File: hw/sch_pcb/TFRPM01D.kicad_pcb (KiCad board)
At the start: 2 copper layers, 37.5 x 19 mm, 28 parts, among them J1 HEADER_1x03, J2 SM04B-GHS-TB, J3 SM04B-GHS-TB, M2 M3, U1 PCF8583, U2 SN74LVC1G14-Q1, U3 MIC5504-3.3YM5

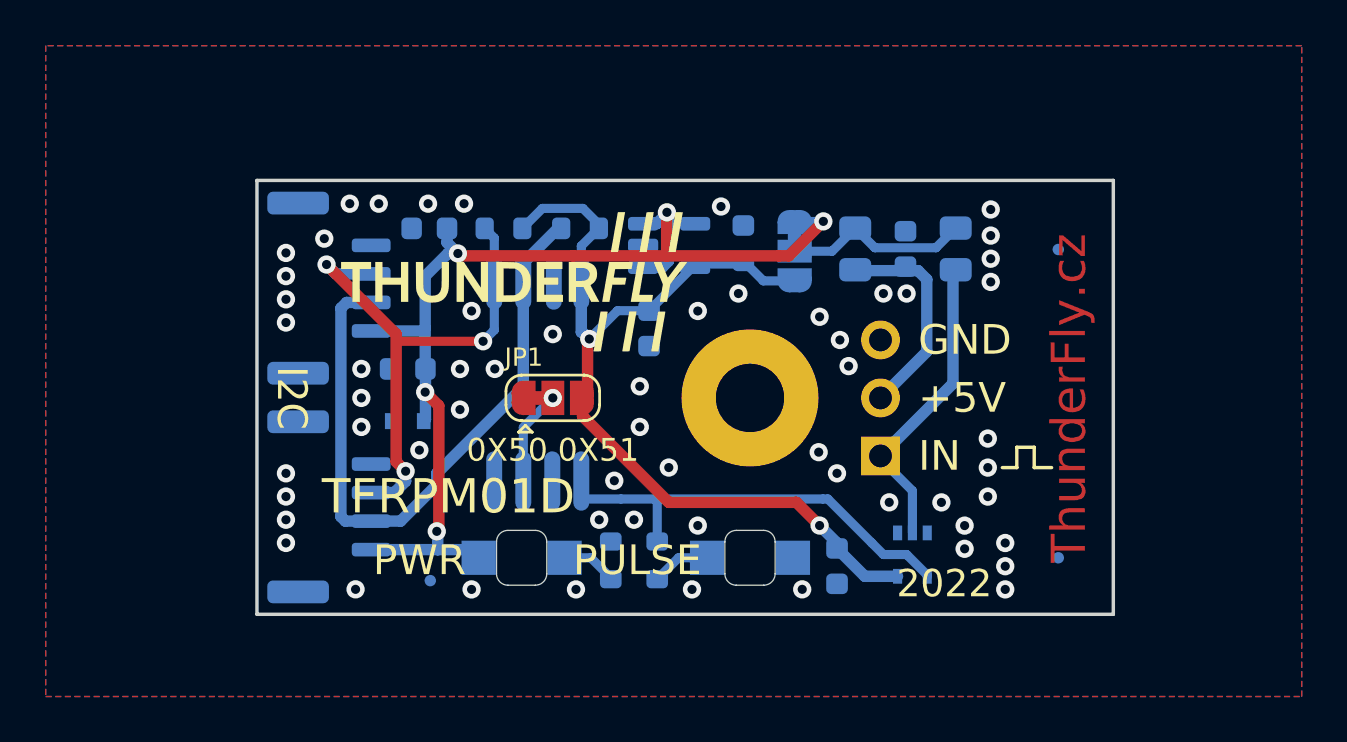
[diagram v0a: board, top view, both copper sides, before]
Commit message: Graphics and layout improvements. Net classes for default and power set.
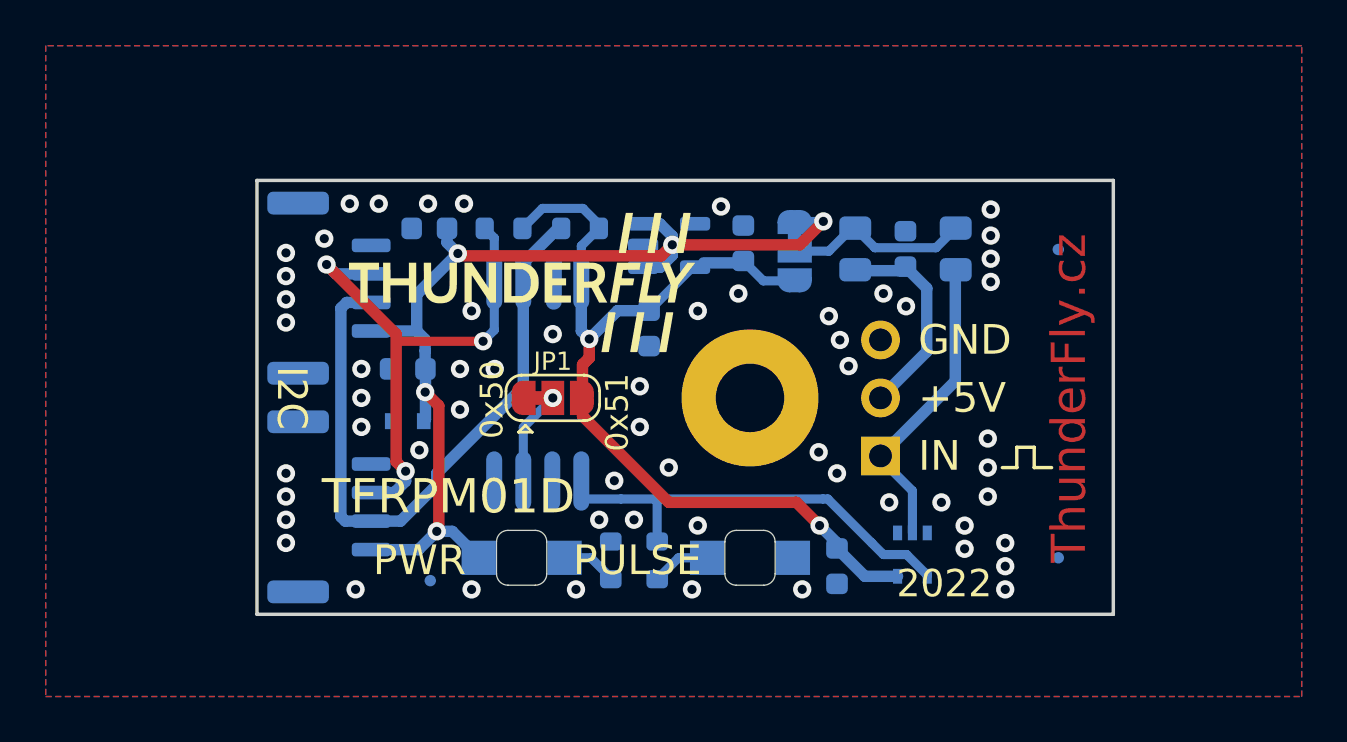
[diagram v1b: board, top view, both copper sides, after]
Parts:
- moved G1 0.35 mm to (122.5, 127.3)
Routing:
- net +5V: track 49.5 -> 46.2 mm
- net +3V3: track 39.6 -> 41.0 mm
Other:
- board text added: "0x50"
- board text added: "0x51"
- board text removed: "0X50 0X51"

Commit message: Repair #30
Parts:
- moved C2 0.27 mm to (139.2, 126.0)
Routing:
- net +5V: track 46.2 -> 43.7 mm
- net /SCL: track 29.7 -> 31.7 mm
- net +3V3: track 41.0 -> 40.4 mm
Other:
- board text added: "0x50 0x51"
- board text removed: "0x50"
- board text removed: "0x51"

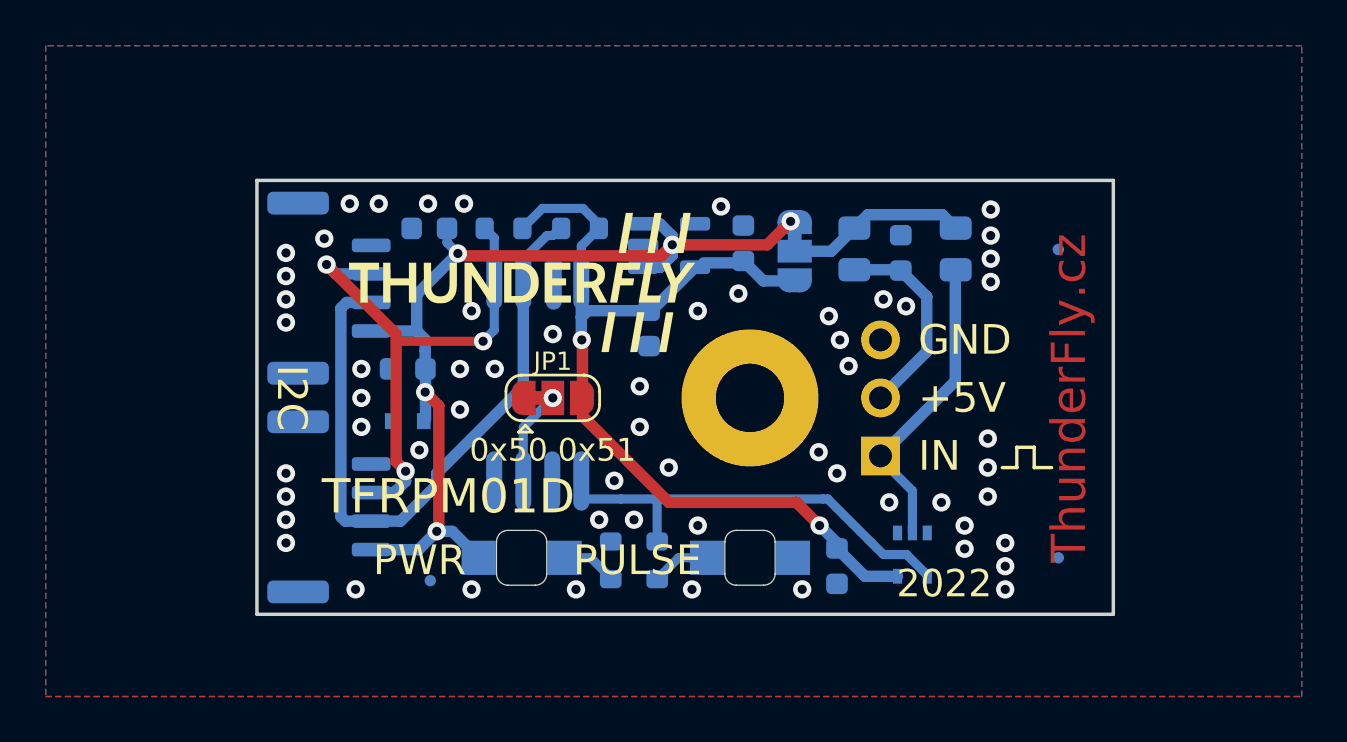
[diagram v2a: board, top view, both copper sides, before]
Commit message: Silkscreen modification
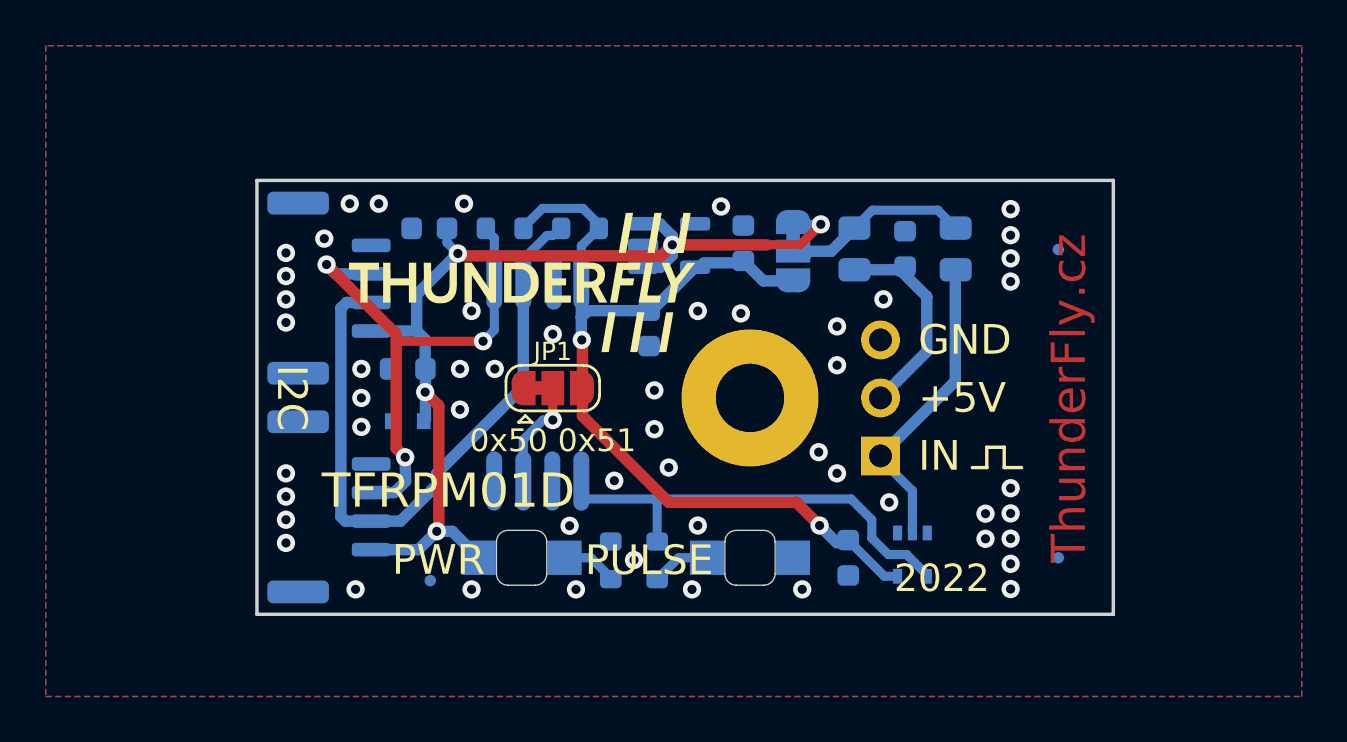
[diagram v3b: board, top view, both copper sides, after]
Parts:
- moved C6 0.61 mm to (136.9, 139.3)
- moved JP1 0.43 mm to (124.0, 131.9)
- moved C2 0.26 mm to (139.4, 125.8)
- moved JP2 0.07 mm to (134.5, 125.9)
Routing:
- net /SCL: track 31.7 -> 27.4 mm
- net +5V: track 43.7 -> 44.8 mm
- net +3V3: track 40.4 -> 39.4 mm
- net Net-(JP1-Pad2): track 4.17 -> 4.86 mm
- net GND: vias 58 -> 52

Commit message: Improve silkscreen.
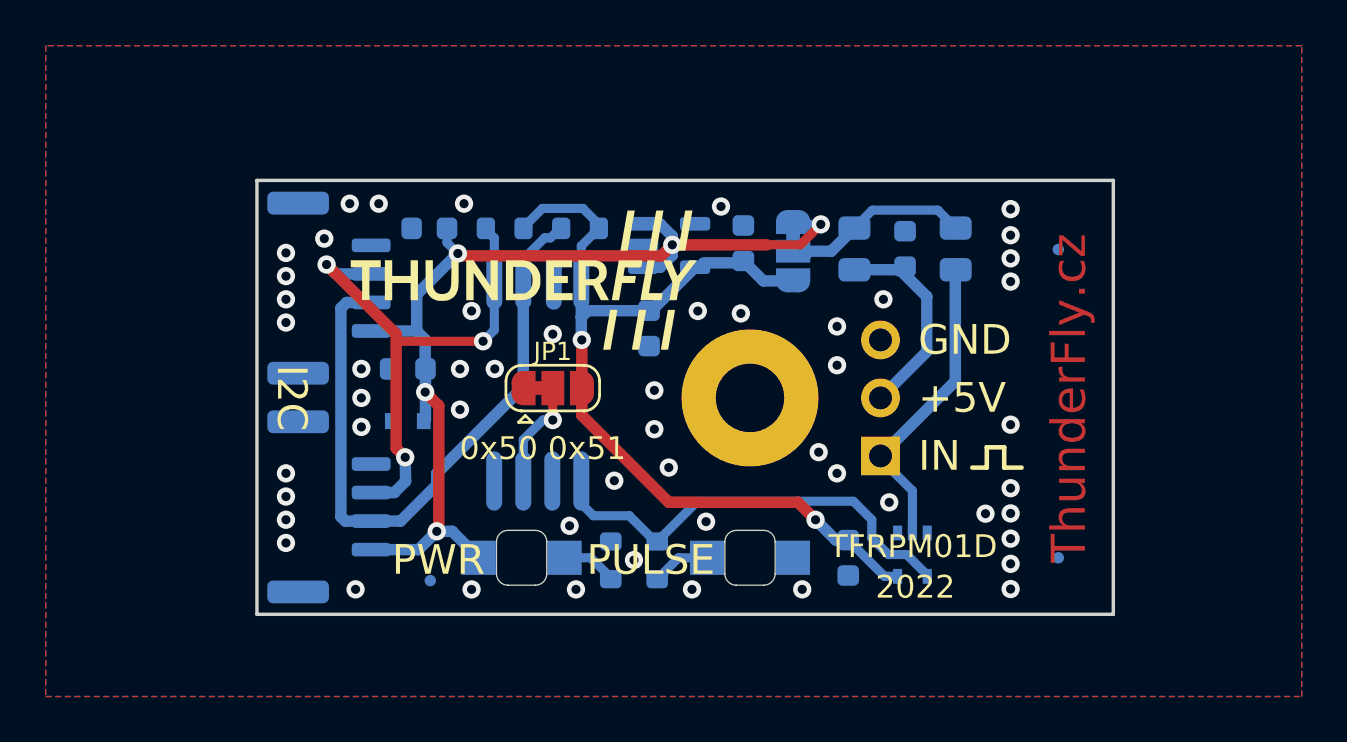
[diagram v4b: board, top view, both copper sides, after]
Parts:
- moved G1 0.13 mm to (122.6, 127.2)
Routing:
- net Net-(R4-Pad1): track 18.9 -> 19.6 mm

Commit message: Improve layout uniform track widts. Resolve DRC and ERC issues.
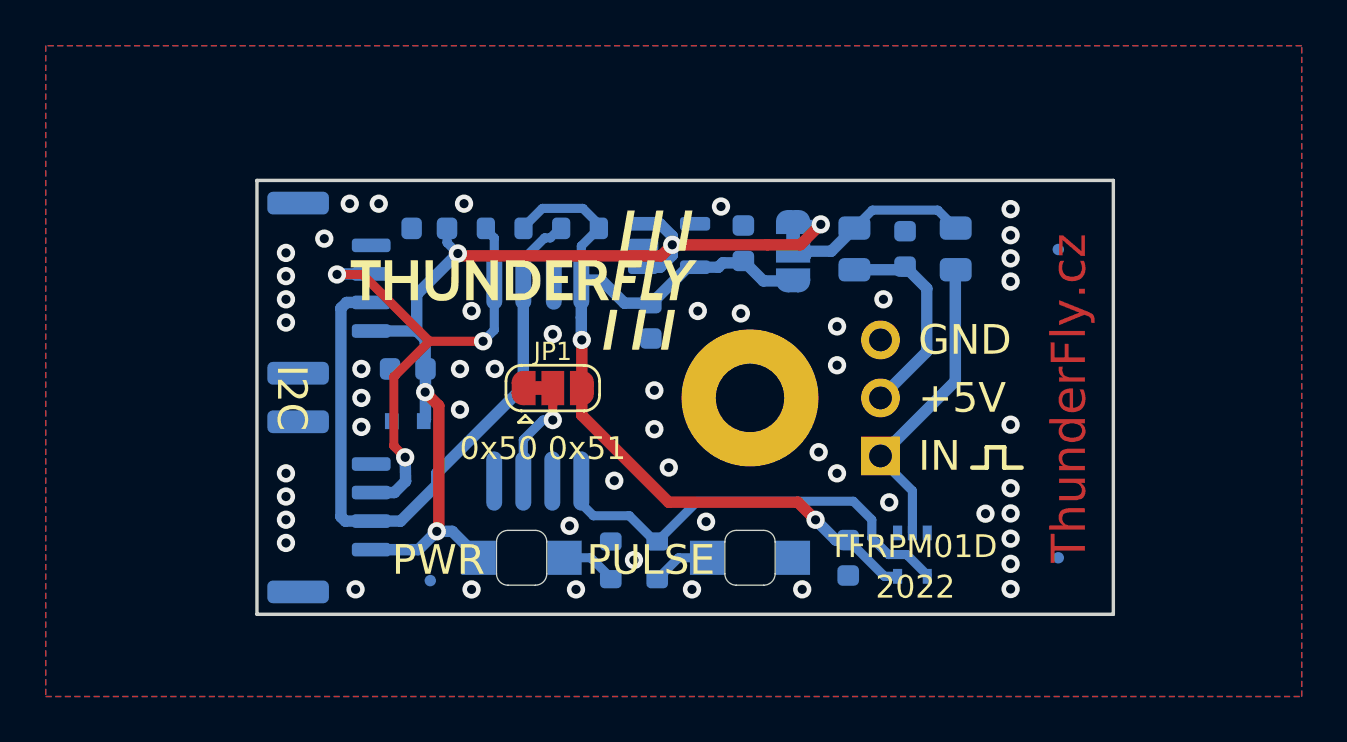
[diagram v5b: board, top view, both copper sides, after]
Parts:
- moved C5 0.34 mm to (128.2, 129.0)
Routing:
- net +3V3: track 39.9 -> 40.6 mm
- net /SDA: track 23.7 -> 23.1 mm
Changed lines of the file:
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@@
   )
   (footprint "Capacitor_SMD:C_0603_1608Metric" (layer "B.Cu")
-    (at 128.1685 129.286 -90)
+    (at 128.2446 128.9558 -90)
     (descr "Capacitor SMD 0603 (1608 Metric), square (rectangular) end terminal, IPC_7351 nominal, (Body size source: IPC-SM-782 page 76, https://www.pcb-3d.com/wordpress/wp-content/uploads/ipc-sm-782a_amendment_1_and_2.pdf), generated with kicad-footprint-generator")
     (tags "capacitor")
@@
   (via (at 125.222 129.791096) (size 0.8) (drill 0.4) (layers "F.Cu" "B.Cu") (net 4))
   (via (at 135.4582 137.668) (size 0.8) (drill 0.4) (layers "F.Cu" "B.Cu") (net 4))
-  (segment (start 125.486096 128.511) (end 125.201 128.796096) (width 0.5) (layer "B.Cu") (net 4))
   (segment (start 125.201 127.956) (end 125.201 125.676) (width 0.4) (layer "B.Cu") (net 4))
+  (segment (start 131.394 126.416) (end 131.999 126.416) (width 0.5) (layer "B.Cu") (net 4))
   (segment (start 125.201 129.770096) (end 125.201 128.796096) (width 0.5) (layer "B.Cu") (net 4))
   (segment (start 125.201 128.796096) (end 125.201 127.169096) (width 0.5) (layer "B.Cu") (net 4))
   (segment (start 139.05 140.142) (end 138.473904 140.142) (width 0.4) (layer "B.Cu") (net 4))
-  (segment (start 130.556 126.416) (end 131.999 126.416) (width 0.5) (layer "B.Cu") (net 4))
+  (segment (start 128.283 128.1808) (end 129.8578 126.606) (width 0.5) (layer "B.Cu") (net 4))
   (segment (start 136.346296 138.556096) (end 135.4582 137.668) (width 0.5) (layer "B.Cu") (net 4))
+  (segment (start 127.0886 128.1808) (end 128.2446 128.1808) (width 0.5) (layer "B.Cu") (net 4))
   (segment (start 125.971 124.731) (end 125.27148 124.03148) (width 0.4) (layer "B.Cu") (net 4))
+  (segment (start 130.1835 126.606) (end 131.204 126.606) (width 0.5) (layer "B.Cu") (net 4))
+  (segment (start 129.8578 126.606) (end 130.1835 126.606) (width 0.5) (layer "B.Cu") (net 4))
   (segment (start 134.546 127.206) (end 133.171 127.206) (width 0.5) (layer "B.Cu") (net 4))
   (segment (start 125.27148 124.03148) (end 123.49552 124.03148) (width 0.4) (layer "B.Cu") (net 4))
+  (segment (start 126.076896 127.169096) (end 127.0886 128.1808) (width 0.5) (layer "B.Cu") (net 4))
   (segment (start 125.201 125.676) (end 125.971 124.906) (width 0.4) (layer "B.Cu") (net 4))
-  (segment (start 128.2785 128.511) (end 130.1835 126.606) (width 0.5) (layer "B.Cu") (net 4))
-  (segment (start 128.1685 128.511) (end 125.486096 128.511) (width 0.5) (layer "B.Cu") (net 4))
+  (segment (start 128.2446 128.1808) (end 128.283 128.1808) (width 0.5) (layer "B.Cu") (net 4))
+  (segment (start 125.201 127.169096) (end 126.076896 127.169096) (width 0.5) (layer "B.Cu") (net 4))
+  (segment (start 131.204 126.606) (end 131.394 126.416) (width 0.5) (layer "B.Cu") (net 4))
   (segment (start 123.49552 124.03148) (end 122.621 124.906) (width 0.4) (layer "B.Cu") (net 4))
   (segment (start 138.473904 140.142) (end 136.888 138.556096) (width 0.4) (layer "B.Cu") (net 4))
   (segment (start 136.888 138.556096) (end 136.346296 138.556096) (width 0.5) (layer "B.Cu") (net 4))
-  (segment (start 125.222 129.791096) (end 125.201 129.770096) (width 0.5) (layer "B.Cu") (net 4))
   (segment (start 133.171 127.206) (end 132.296 126.331) (width 0.5) (layer "B.Cu") (net 4))
   (segment (start 119.796 126.006) (end 119.901 126.111) (width 0.5) (layer "F.Cu") (net 5))
@@
   (segment (start 119.901 126.111) (end 128.698896 126.111) (width 0.5) (layer "F.Cu") (net 5))
   (segment (start 118.872 138.173096) (end 118.959511 138.085585) (width 0.5) (layer "F.Cu") (net 5))
-  (segment (start 133.340504 125.625496) (end 134.7936 125.625496) (width 0.4) (layer "F.Cu") (net 5))
-  (segment (start 134.7936 125.625496) (end 135.688 124.731096) (width 0.4) (layer "F.Cu") (net 5))
+  (segment (start 133.340504 125.625496) (end 134.7936 125.625496) (width 0.5) (layer "F.Cu") (net 5))
   (segment (start 133.340504 125.625496) (end 129.1844 125.625496) (width 0.5) (layer "F.Cu") (net 5))
+  (segment (start 134.7936 125.625496) (end 135.688 124.731096) (width 0.5) (layer "F.Cu") (net 5))
   (segment (start 128.698896 126.111) (end 129.1844 125.625496) (width 0.5) (layer "F.Cu") (net 5))
   (segment (start 118.959511 138.085585) (end 118.959511 132.672607) (width 0.5) (layer "F.Cu") (net 5))
@@
   (segment (start 119.321 124.906) (end 119.321 125.531) (width 0.4) (layer "B.Cu") (net 5))
   (segment (start 116 129.4) (end 117.993096 129.4) (width 0.5) (layer "B.Cu") (net 5))
-  (segment (start 117.094 129.537096) (end 114.046 126.489096) (width 0.5) (layer "F.Cu") (net 6))
-  (segment (start 117.094 134.537096) (end 117.488 134.931096) (width 0.5) (layer "F.Cu") (net 6))
-  (segment (start 117.094 129.537096) (end 117.094 134.537096) (width 0.5) (layer "F.Cu") (net 6))
-  (segment (start 120.9 129.85) (end 117.24 129.85) (width 0.4) (layer "F.Cu") (net 6))
+  (segment (start 116.9924 131.4046) (end 118.547 129.85) (width 0.4) (layer "F.Cu") (net 6))
+  (segment (start 117.488 134.931096) (end 116.9924 134.435496) (width 0.4) (layer "F.Cu") (net 6))
+  (segment (start 115.6208 126.9238) (end 114.5032 126.9238) (width 0.4) (layer "F.Cu") (net 6))
+  (segment (start 116.9924 134.435496) (end 116.9924 131.4046) (width 0.4) (layer "F.Cu") (net 6))
+  (segment (start 118.547 129.85) (end 120.9 129.85) (width 0.4) (layer "F.Cu") (net 6))
+  (segment (start 118.547 129.85) (end 115.6208 126.9238) (width 0.4) (layer "F.Cu") (net 6))
   (via (at 117.488 134.931096) (size 0.8) (drill 0.4) (layers "F.Cu" "B.Cu") (net 6))
-  (via (at 114.046 126.489096) (size 0.8) (drill 0.4) (layers "F.Cu" "B.Cu") (net 6))
+  (via (at 114.5032 126.9238) (size 0.8) (drill 0.4) (layers "F.Cu" "B.Cu") (net 6))
   (via (at 120.9 129.85) (size 0.8) (drill 0.4) (layers "F.Cu" "B.Cu") (net 6))
   (segment (start 117.488 134.931096) (end 117.508764 135.980332) (width 0.5) (layer "B.Cu") (net 6))
@@
   (segment (start 121.391 129.359) (end 120.9 129.85) (width 0.4) (layer "B.Cu") (net 6))
   (segment (start 117.014096 136.475) (end 116 136.475) (width 0.5) (layer "B.Cu") (net 6))
-  (segment (start 114.456904 126.9) (end 114.046 126.489096) (width 0.5) (layer "B.Cu") (net 6))
-  (segment (start 116 126.9) (end 114.456904 126.9) (width 0.5) (layer "B.Cu") (net 6))
   (segment (start 121.391 127.956) (end 121.391 125.326) (width 0.4) (layer "B.Cu") (net 6))
+  (segment (start 114.527 126.9) (end 114.5032 126.9238) (width 0.5) (layer "B.Cu") (net 6))
+  (segment (start 116 126.9) (end 114.527 126.9) (width 0.5) (layer "B.Cu") (net 6))
   (segment (start 121.391 125.326) (end 120.971 124.906) (width 0.4) (layer "B.Cu") (net 6))
   (segment (start 121.391 127.956) (end 121.391 129.359) (width 0.4) (layer "B.Cu") (net 6))
@@
   (segment (start 137.922 137.665096) (end 137.922 138.465096) (width 0.4) (layer "B.Cu") (net 8))
   (segment (start 125.73 137.4902) (end 125.201 136.9612) (width 0.4) (layer "B.Cu") (net 8))
-  (segment (start 128.524 138.618096) (end 128.716904 138.618096) (width 0.4) (layer "B.Cu") (net 8))
   (segment (start 138.646 139.189096) (end 139.446 139.189096) (width 0.4) (layer "B.Cu") (net 8))
   (segment (start 123.952 133.3) (end 123.952 131.9) (width 0.4) (layer "F.Cu") (net 9))
@@
   (segment (start 135.031 125.984) (end 135.031 126.081) (width 0.5) (layer "B.Cu") (net 10))
   (segment (start 135.031 126.081) (end 135.001 126.111) (width 0.5) (layer "B.Cu") (net 10))
+  (segment (start 139.192 126.756096) (end 139.553096 126.756096) (width 0.5) (layer "B.Cu") (net 11))
   (segment (start 137.16 126.7185) (end 139.154404 126.7185) (width 0.5) (layer "B.Cu") (net 11))
-  (segment (start 140.329489 127.893585) (end 140.329489 130.304607) (width 0.5) (layer "B.Cu") (net 11))
-  (segment (start 139.192 126.756096) (end 140.329489 127.893585) (width 0.5) (layer "B.Cu") (net 11))
-  (segment (start 138.303 132.331096) (end 140.329489 130.304607) (width 0.5) (layer "B.Cu") (net 11))
+  (segment (start 139.553096 126.756096) (end 140.329489 127.532489) (width 0.5) (layer "B.Cu") (net 11))
+  (segment (start 140.329489 127.532489) (end 140.329489 130.304607) (width 0.5) (layer "B.Cu") (net 11))
+  (segment (start 140.329489 130.304607) (end 138.303 132.331096) (width 0.5) (layer "B.Cu") (net 11))
   (segment (start 125.618 139.331096) (end 124.468 139.331096) (width 0.4) (layer "B.Cu") (net 12))
   (segment (start 126.492 140.205096) (end 125.618 139.331096) (width 0.4) (layer "B.Cu") (net 12))
